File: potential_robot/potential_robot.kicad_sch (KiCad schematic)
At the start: 8 parts, among them U1 LM741, U2 LM741

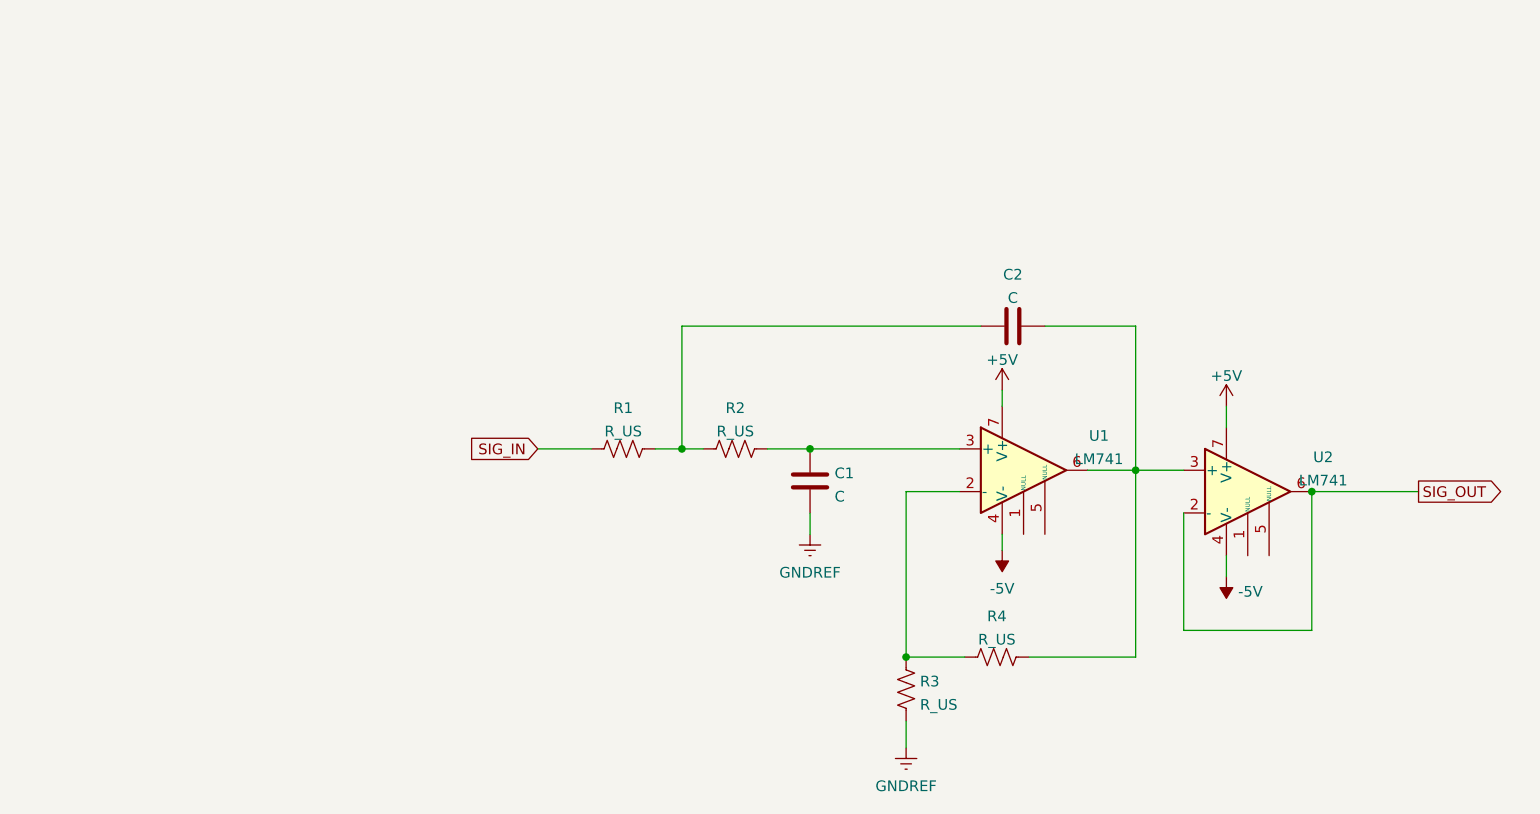
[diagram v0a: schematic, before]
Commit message: Replaced a resistor with a pot for volume control. Added a power jack, rectifier and smoother TBD.
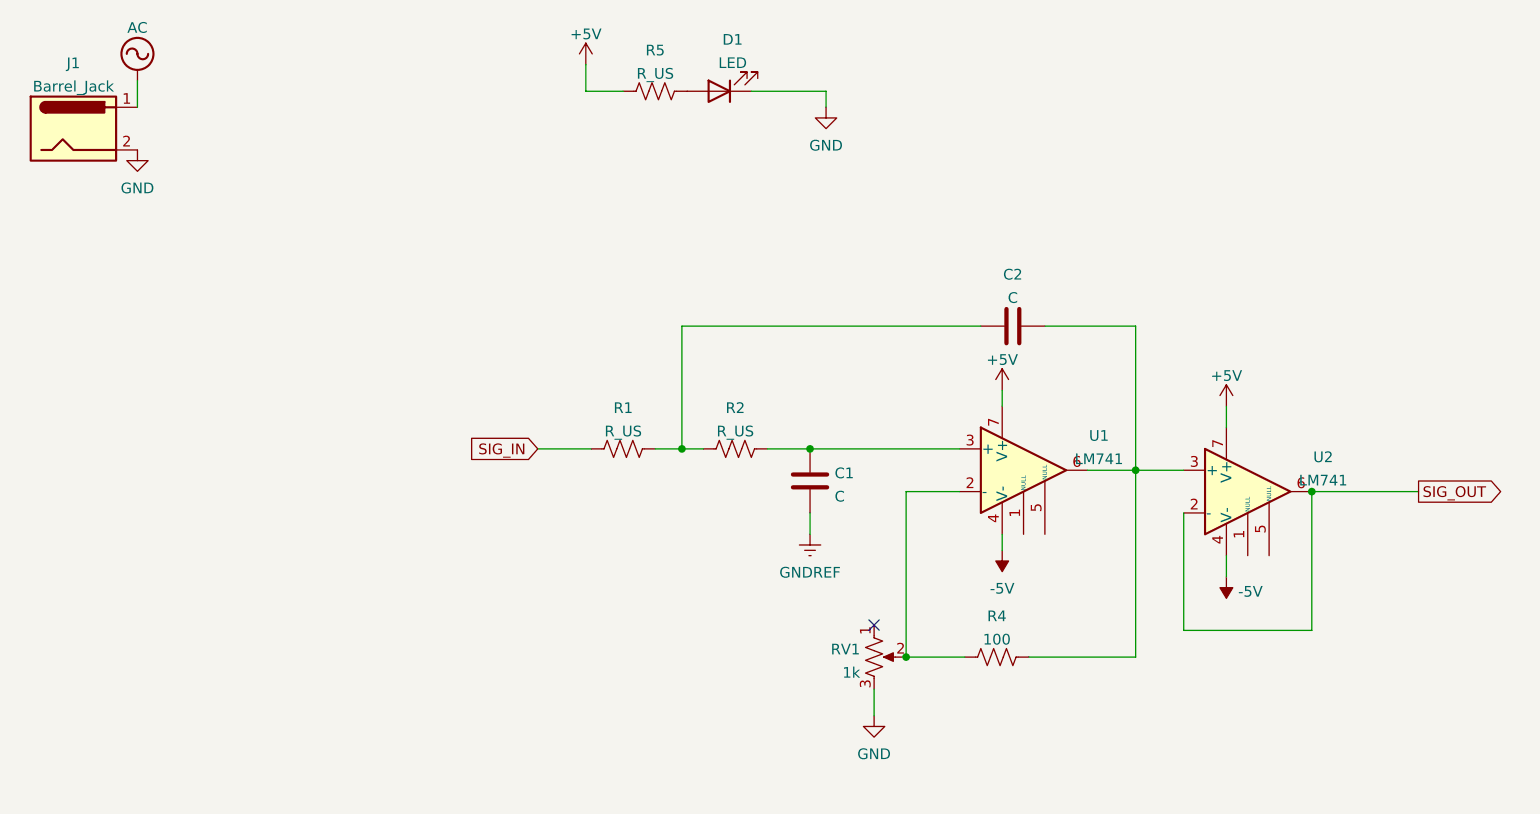
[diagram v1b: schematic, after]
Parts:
- removed R3: R_US, Resistor_THT:R_Axial_DIN0207_L6.3mm_D2.5mm_P7.62mm_Horizontal, symbol Device:R_US
- added D1: LED, LED_SMD:LED_0805_2012Metric, symbol Device:LED
- added J1: Barrel_Jack, Connector_BarrelJack:BarrelJack_Wuerth_6941xx301002, symbol Connector:Barrel_Jack
- added R5: R_US, Resistor_THT:R_Axial_DIN0207_L6.3mm_D2.5mm_P7.62mm_Horizontal, symbol Device:R_US
- added RV1: 1k, Potentiometer_THT:Potentiometer_ACP_CA6-H2,5_Horizontal, symbol Device:R_Potentiometer_US
- R4: value R_US -> 100
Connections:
- net +5V: now also R5.1
- net at R4.1, U1.2 (-): now also RV1.2
- new net: D1.2 (A), R5.2
- new net AC: J1.1
- new net GND: D1.1 (K), J1.2, RV1.3
- no-connect marks 0 -> 1
